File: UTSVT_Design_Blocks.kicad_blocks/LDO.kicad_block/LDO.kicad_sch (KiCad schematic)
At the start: 3 parts

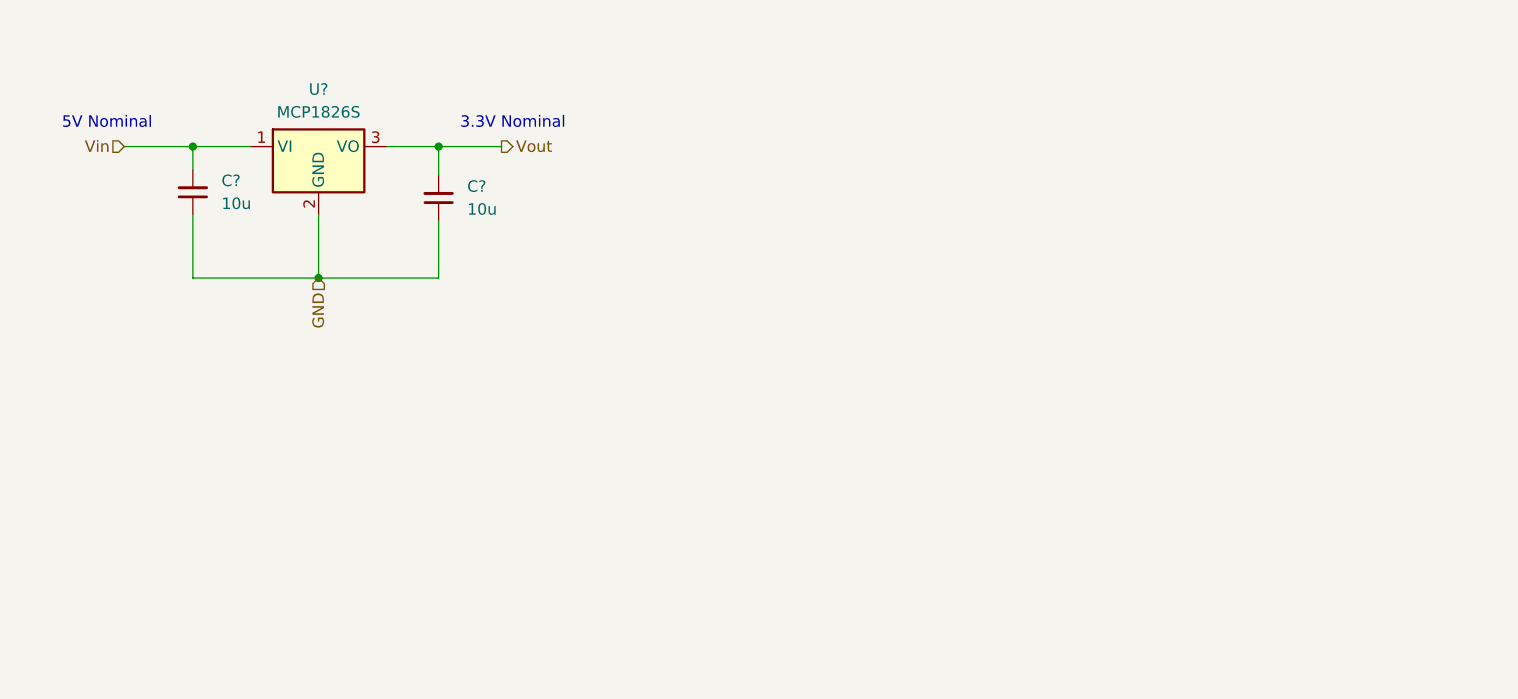
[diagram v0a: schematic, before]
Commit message: added reverse current diode and some datasheet values for designers
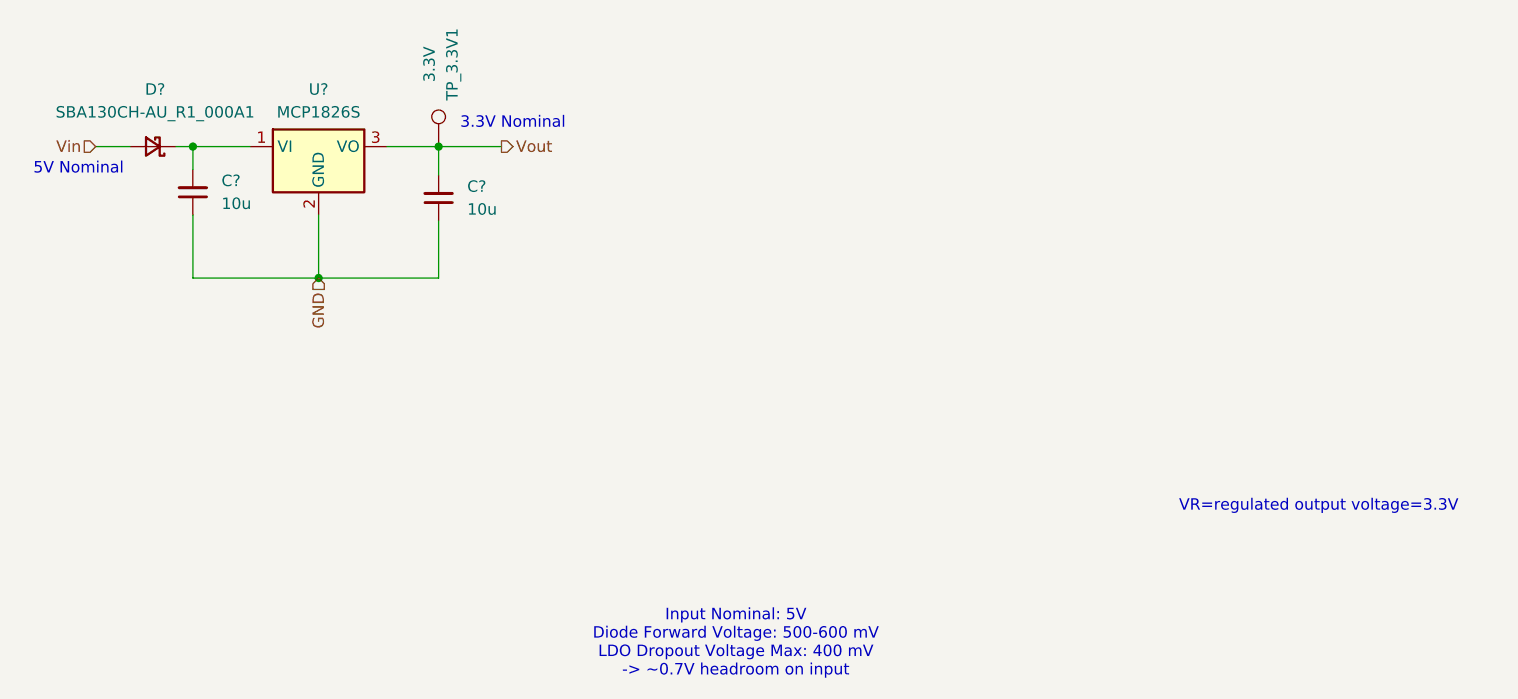
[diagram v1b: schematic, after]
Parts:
- added D?: SBA130CH-AU_R1_000A1, Diode_SMD:D_SOD-323_HandSoldering, symbol Device:D_Schottky_Small
- added TP_3.3V1: 3.3V, TestPoint:TestPoint_Loop_D1.80mm_Drill1.0mm_Beaded, symbol Connector:TestPoint
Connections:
- net Vin: now also D?.2 (A); no longer C?.2, U?.1 (VI)
- net Vout: now also TP_3.3V1.1
- new net: C?.2, D?.1 (K), U?.1 (VI)
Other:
- note added: "Input Nominal: 5V Diode Forward Voltage: 500-600 mV LDO Dropout Voltage Max: 400 mV -> ~0.7V headroom on input"
- note added: "VR=regulated output voltage=3.3V"
